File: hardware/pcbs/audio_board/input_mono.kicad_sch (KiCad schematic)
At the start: 3 parts, among them J3 Stereo Line-in

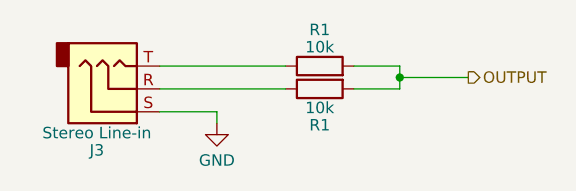
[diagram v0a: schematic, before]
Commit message: Small audio board fixes and add DHAN-M module
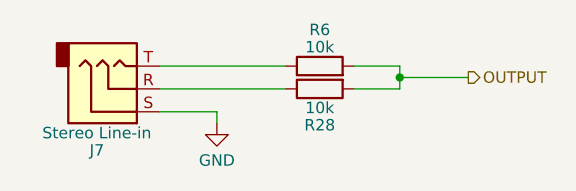
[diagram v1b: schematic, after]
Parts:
- renumbered J3 to J7, R1 to R28, R1 to R6

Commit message: audio_board, power_board: update shop and part links
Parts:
- J7: Part (none) -> SJ1-3533NG; Shop (none) -> https://eu.mouser.com/ProductDetail/490-SJ1-3533NG
- R28, R6: Part (none) -> R 10kΩ 0603
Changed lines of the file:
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@@
+			)
+		)
+		(property "Part" "R 10kΩ 0603"
+			(at 105.41 93.98 0)
+			(effects
+				(font
+					(size 1.27 1.27)
+				)
+				(hide yes)
 			)
 		)
@@
 		)
 		(property "MPN" "490-SJ1-3533NG"
+			(at 82.55 96.52 0)
+			(effects
+				(font
+					(size 1.27 1.27)
+				)
+				(hide yes)
+			)
+		)
+		(property "Part" " SJ1-3533NG "
+			(at 82.55 96.52 0)
+			(effects
+				(font
+					(size 1.27 1.27)
+				)
+				(hide yes)
+			)
+		)
+		(property "Shop" "https://eu.mouser.com/ProductDetail/490-SJ1-3533NG"
 			(at 82.55 96.52 0)
 			(effects
@@
 			(at 105.41 96.52 0)
 			(effects
+				(font
+					(size 1.27 1.27)
+				)
+				(hide yes)
+			)
+		)
+		(property "Part" "R 10kΩ 0603"
+			(at 105.41 96.52 0)
+			(effects

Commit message: Audio board Rev. C fixes
* Switch opamp to OPA1678
* Fix filter resistor on inputs from 22 ohm to 220 ohm
* Make the board 4 layers for a better ground plane
* Implement an RC filter for the opamp 5V line
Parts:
- R28, R6: MPN (none) -> 560112116023
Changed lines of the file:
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@@
+			)
+		)
+		(property "MPN" "560112116023 "
+			(at 105.41 93.98 0)
+			(effects
+				(font
+					(size 1.27 1.27)
+				)
+				(hide yes)
 			)
 		)
@@
 			(at 105.41 96.52 0)
 			(effects
+				(font
+					(size 1.27 1.27)
+				)
+				(hide yes)
+			)
+		)
+		(property "MPN" "560112116023 "
+			(at 105.41 96.52 0)
+			(effects

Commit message: pcbs: update purchase info
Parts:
- R28, R6: Part R 10kΩ 0603 -> R 10kΩ 125mW 1% 0603; Shop (none) -> https://store.comet.bg/Catalogue/Product/4415/
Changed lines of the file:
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@@
 			)
 		)
-		(property "Part" "R 10kΩ 0603"
+		(property "Part" "R 10kΩ 125mW 1% 0603"
 			(at 105.41 93.98 0)
 			(effects
@@
 		)
 		(property "MPN" "560112116023 "
+			(at 105.41 93.98 0)
+			(effects
+				(font
+					(size 1.27 1.27)
+				)
+				(hide yes)
+			)
+		)
+		(property "Shop" "https://store.comet.bg/Catalogue/Product/4415/"
 			(at 105.41 93.98 0)
 			(effects
@@
 			)
 		)
-		(property "Part" "R 10kΩ 0603"
+		(property "Part" "R 10kΩ 125mW 1% 0603"
 			(at 105.41 96.52 0)
 			(effects
@@
 			(at 105.41 96.52 0)
 			(effects
+				(font
+					(size 1.27 1.27)
+				)
+				(hide yes)
+			)
+		)
+		(property "Shop" "https://store.comet.bg/Catalogue/Product/4415/"
+			(at 105.41 96.52 0)
+			(effects

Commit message: WIP
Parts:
- R28, R6: footprint Resistor_SMD:R_0603_1608Metric_Pad0.98x0.95mm_HandSolder -> Resistor_SMD:R_0805_2012Metric
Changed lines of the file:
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@@
 (kicad_sch
-	(version 20231120)
+	(version 20250114)
 	(generator "eeschema")
-	(generator_version "8.0")
+	(generator_version "9.0")
 	(paper "A4")
 	(junction
@@
 		(shape output)
 		(at 121.92 95.25 0)
-		(fields_autoplaced yes)
 		(effects
 			(font
@@
 			)
 		)
-		(property "Footprint" "Resistor_SMD:R_0603_1608Metric_Pad0.98x0.95mm_HandSolder"
+		(property "Footprint" "Resistor_SMD:R_0805_2012Metric"
 			(at 105.41 95.758 90)
 			(effects
@@
 			)
 		)
-		(property "Footprint" "Resistor_SMD:R_0603_1608Metric_Pad0.98x0.95mm_HandSolder"
+		(property "Footprint" "Resistor_SMD:R_0805_2012Metric"
 			(at 105.41 94.742 90)
 			(effects
